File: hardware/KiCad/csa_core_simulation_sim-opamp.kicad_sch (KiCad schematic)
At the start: 3 parts

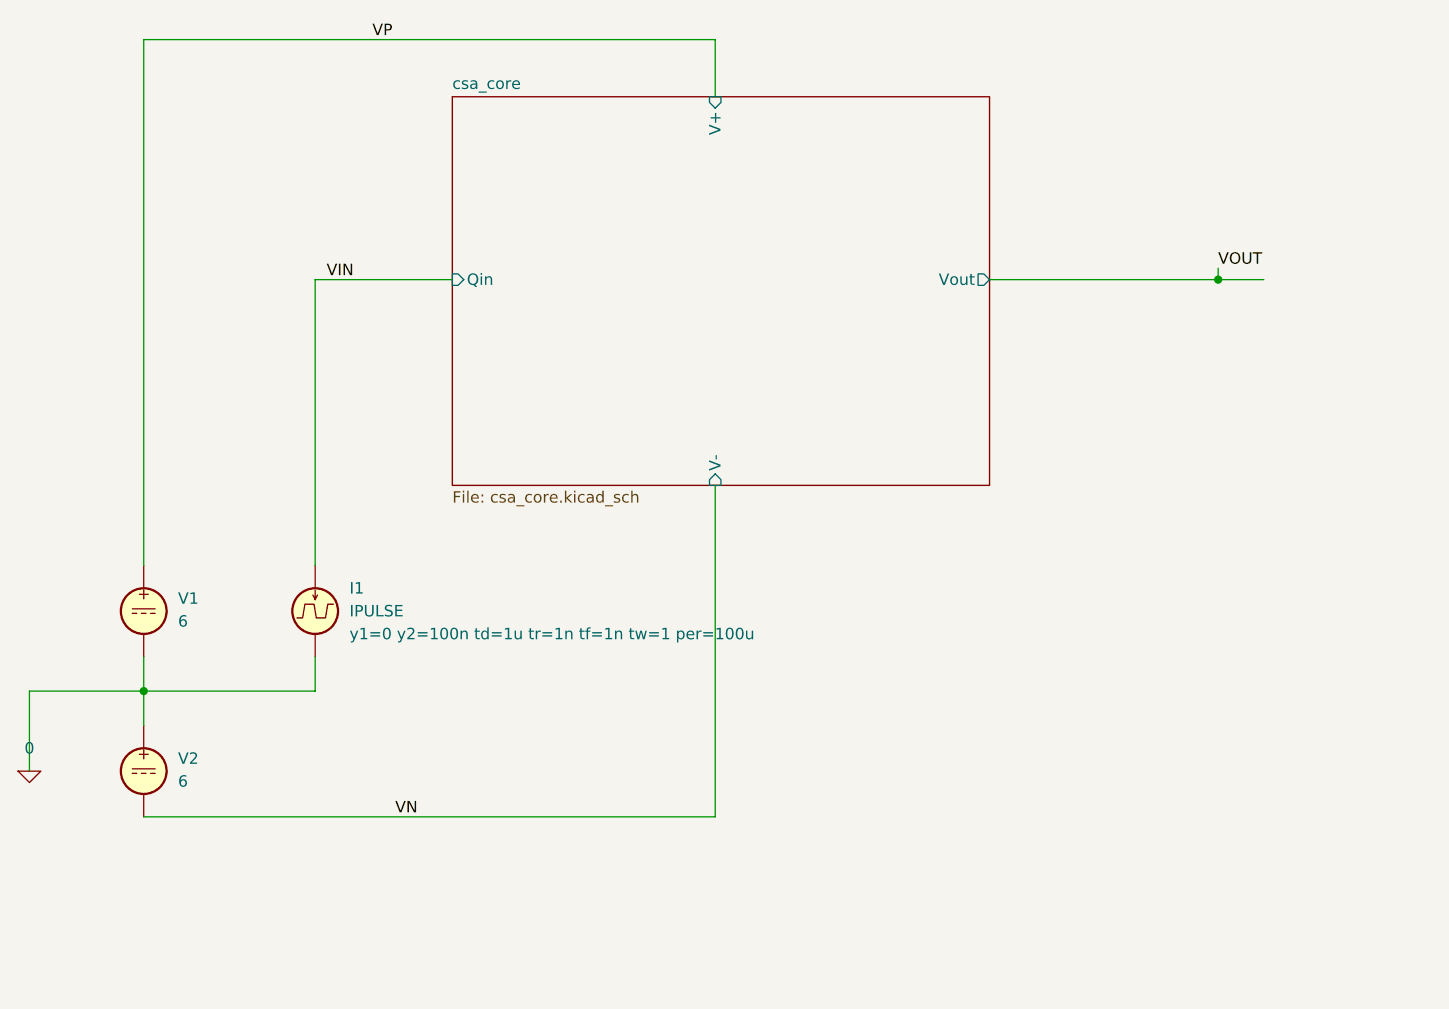
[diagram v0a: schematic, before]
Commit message: Added lead-lag compenstation after JFET which seems to stabilize loop in simulation. Added CR-RC shaping/amplification. Committing changes before starting simulation of shapers
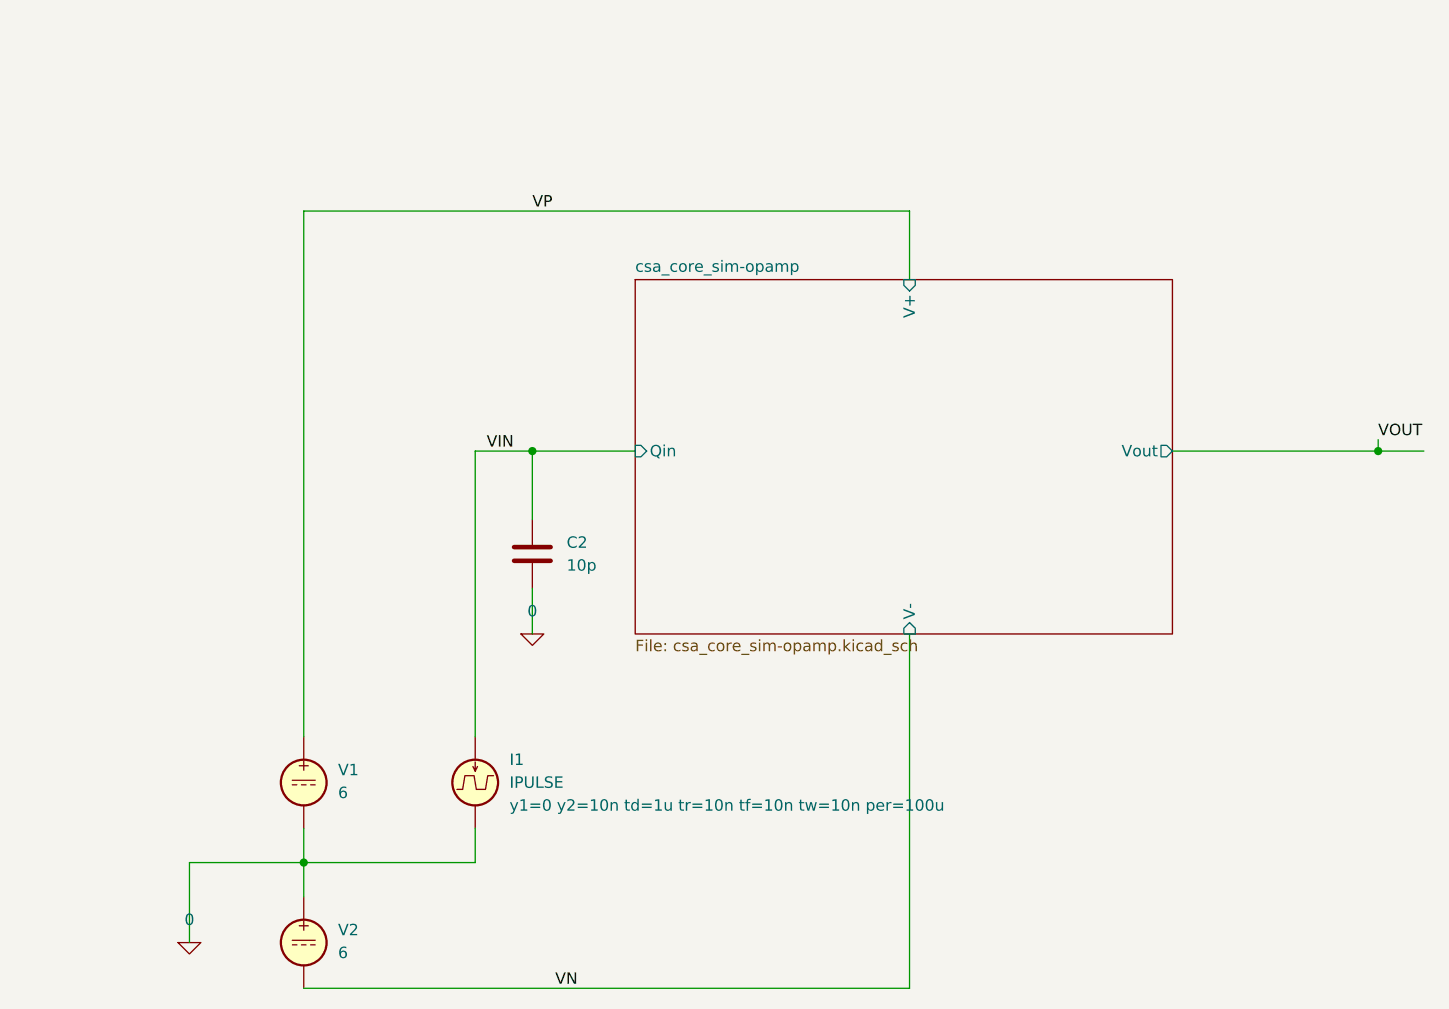
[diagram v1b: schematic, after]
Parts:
- added C2: 10p, symbol Device:C
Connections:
- net 0: now also C2.2
- net VIN: now also C2.1
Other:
- removed sheet csa_core
- added sheet csa_core_sim-opamp (csa_core_sim-opamp.kicad_sch)

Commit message: End of day save. Just needs voids added to planes to reduce capacitance
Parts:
- added R12: 1 Meg, symbol Device:R
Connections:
- net 0: now also R12.2
- net VOUT: now also R12.1
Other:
- sheet csa_core_sim-opamp ports: added vout; removed Vout
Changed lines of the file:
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@@
 	(paper "A4")
+	(junction
+		(at 177.8 87.63)
+		(diameter 0)
+		(color 0 0 0 0)
+	)
 	(junction
 		(at 186.69 87.63)
@@
 	(wire
 		(pts
+			(xy 177.8 102.87) (xy 177.8 110.49)
+		)
+		(stroke
+			(width 0)
+			(type default)
+		)
+	)
+	(wire
+		(pts
 			(xy 134.62 60.96) (xy 134.62 68.58)
 		)
@@
 	(wire
 		(pts
+			(xy 177.8 87.63) (xy 186.69 87.63)
+		)
+		(stroke
+			(width 0)
+			(type default)
+		)
+	)
+	(wire
+		(pts
 			(xy 67.31 147.32) (xy 134.62 147.32)
 		)
@@
 	(wire
 		(pts
-			(xy 163.83 87.63) (xy 186.69 87.63)
+			(xy 163.83 87.63) (xy 177.8 87.63)
 		)
 		(stroke
@@
 		(pts
 			(xy 92.71 102.87) (xy 92.71 107.95)
+		)
+		(stroke
+			(width 0)
+			(type default)
+		)
+	)
+	(wire
+		(pts
+			(xy 177.8 87.63) (xy 177.8 95.25)
 		)
 		(stroke
@@
 	)
 	(symbol
+		(lib_id "Device:R")
+		(at 177.8 99.06 0)
+		(unit 1)
+		(exclude_from_sim no)
+		(in_bom yes)
+		(on_board yes)
+		(dnp no)
+		(fields_autoplaced yes)
+		(property "Reference" "R12"
+			(at 180.34 97.7899 0)
+			(effects
+				(font
+					(size 1.27 1.27)
+				)
+				(justify left)
+			)
+		)
+		(property "Value" "1 Meg"
+			(at 180.34 100.3299 0)
+			(effects
+				(font
+					(size 1.27 1.27)
+				)
+				(justify left)
+			)
+		)
+		(property "Footprint" ""
+			(at 176.022 99.06 90)
+			(effects
+				(font
+					(size 1.27 1.27)
+				)
+				(hide yes)
+			)
+		)
+		(property "Datasheet" "~"
+			(at 177.8 99.06 0)
+			(effects
+				(font
+					(size 1.27 1.27)
+				)
+				(hide yes)
+			)
+		)
+		(property "Description" "Resistor"
+			(at 177.8 99.06 0)
+			(effects
+				(font
+					(size 1.27 1.27)
+				)
+				(hide yes)
+			)
+		)
+		(pin "1"
+		)
+		(pin "2"
+		)
+		(instances
+			(project "csa_core_simulation_sim-opamp"
+				(path "/2aaf14b7-a1ca-42e6-b2fb-57bce6369993"
+					(reference "R12")
+					(unit 1)
+				)
+			)
+		)
+	)
+	(symbol
 		(lib_id "Simulation_SPICE:0")
 		(at 54.61 142.24 0)
@@
 				(path "/2aaf14b7-a1ca-42e6-b2fb-57bce6369993"
 					(reference "#GND01")
+					(unit 1)
+				)
+			)
+		)
+	)
+	(symbol
+		(lib_id "Simulation_SPICE:0")
+		(at 177.8 110.49 0)
+		(unit 1)
+		(exclude_from_sim no)
+		(in_bom yes)
+		(on_board yes)
+		(dnp no)
+		(fields_autoplaced yes)
+		(property "Reference" "#GND04"
+			(at 177.8 115.57 0)
+			(effects
+				(font
+					(size 1.27 1.27)
+				)
+				(hide yes)
+			)
+		)
+		(property "Value" "0"
+			(at 177.8 107.95 0)
+			(effects
+				(font
+					(size 1.27 1.27)
+				)
+			)
+		)
+		(property "Footprint" ""
+			(at 177.8 110.49 0)
+			(effects
+				(font
+					(size 1.27 1.27)
+				)
+				(hide yes)
+			)
+		)
+		(property "Datasheet" "https://ngspice.sourceforge.io/docs/ngspice-html-manual/manual.xhtml#subsec_Circuit_elements__device"
+			(at 177.8 120.65 0)
+			(effects
+				(font
+					(size 1.27 1.27)
+				)
+				(hide yes)
+			)
+		)
+		(property "Description" "0V reference potential for simulation"
+			(at 177.8 118.11 0)
+			(effects
+				(font
+					(size 1.27 1.27)
+				)
+				(hide yes)
+			)
+		)
+		(pin "1"
+		)
+		(instances
+			(project "csa_core_simulation_sim-opamp"
+				(path "/2aaf14b7-a1ca-42e6-b2fb-57bce6369993"
+					(reference "#GND04")
 					(unit 1)
 				)
@@
 			)
 		)
-		(pin "Vout" output
+		(pin "vout" input
 			(at 163.83 87.63 0)
 			(effects
